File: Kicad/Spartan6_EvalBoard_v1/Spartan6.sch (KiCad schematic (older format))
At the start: 0 parts

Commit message: Schematic almost done
Schematic almost done, just to connect connector to FPGA
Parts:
- added C? (x3): 100n, ~, symbol C
- added C? (x5): 4.7u, ~, symbol C
- added C? (x4): 470n, ~, symbol C
- added C? (x2): 10u, ~, symbol C
- added FB? (x3): F, ~, symbol F
- added P?: CONN_3X2, symbol CONN_3X2
- added Q? (x5): XC6SLX16, Module, symbol XC6SLX16
- added R? (x2): 1K, ~, symbol R
- added R?: 10K, ~, symbol R
- added U?: FM25V05, ~, symbol FM25V05
- added U?: MX25L8006E, ~, symbol MX25L8006E
- added X?: XOSC, symbol XOSC
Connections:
- net labels added: +1.2V, +3.3V, CLK, FLASH_CSn, FLASH_MISO, FLASH_MOSI, FLASH_SCK, GND, I2C_EE_SCL, I2C_EE_SDA, LED1, LED2, LED3, LED4, TCK, TDI, TDO, TMS
- wire segments 0 -> 154

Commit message: Schematic and netllist created
The correct fpga connection to connector will have to be carried out.
Some more footprints need to be created.
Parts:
- removed Q? (x5): XC6SLX16, Module, symbol XC6SLX16
- added Q401: XC6SLX16, Module, symbol XC6SLX16
- gave numbers to parts that had none: 24
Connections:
- net labels added: 1.2V, 3.3V, IO1, IO10, IO11, IO12, IO13, IO14, IO15, IO16, IO17, IO18, IO19, IO2, IO20, IO21, IO22, IO23, IO24, IO25, IO26, IO27, IO28, IO29, IO3, IO30, IO31, IO32, IO33, IO34, IO35, IO36, IO37, IO38, IO39, IO4, IO40, IO41, IO42, IO43, IO44, IO45, IO46, IO47, IO48, IO49, IO5, IO50, IO51, IO52, IO53, IO54, IO55, IO56, IO57, IO58, IO59, IO6, IO60, IO61, IO62, IO63, IO64, IO65, IO66, IO67, IO68, IO69, IO7, IO70, IO8, IO9, IO[1..70]
- net labels removed: +1.2V, +3.3V
- wire segments 154 -> 223
- no-connect marks 0 -> 81
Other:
- moved on the sheet: C401, C402, C403, C404, C405, C406, C407, C408, C409, C410, C411, C412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

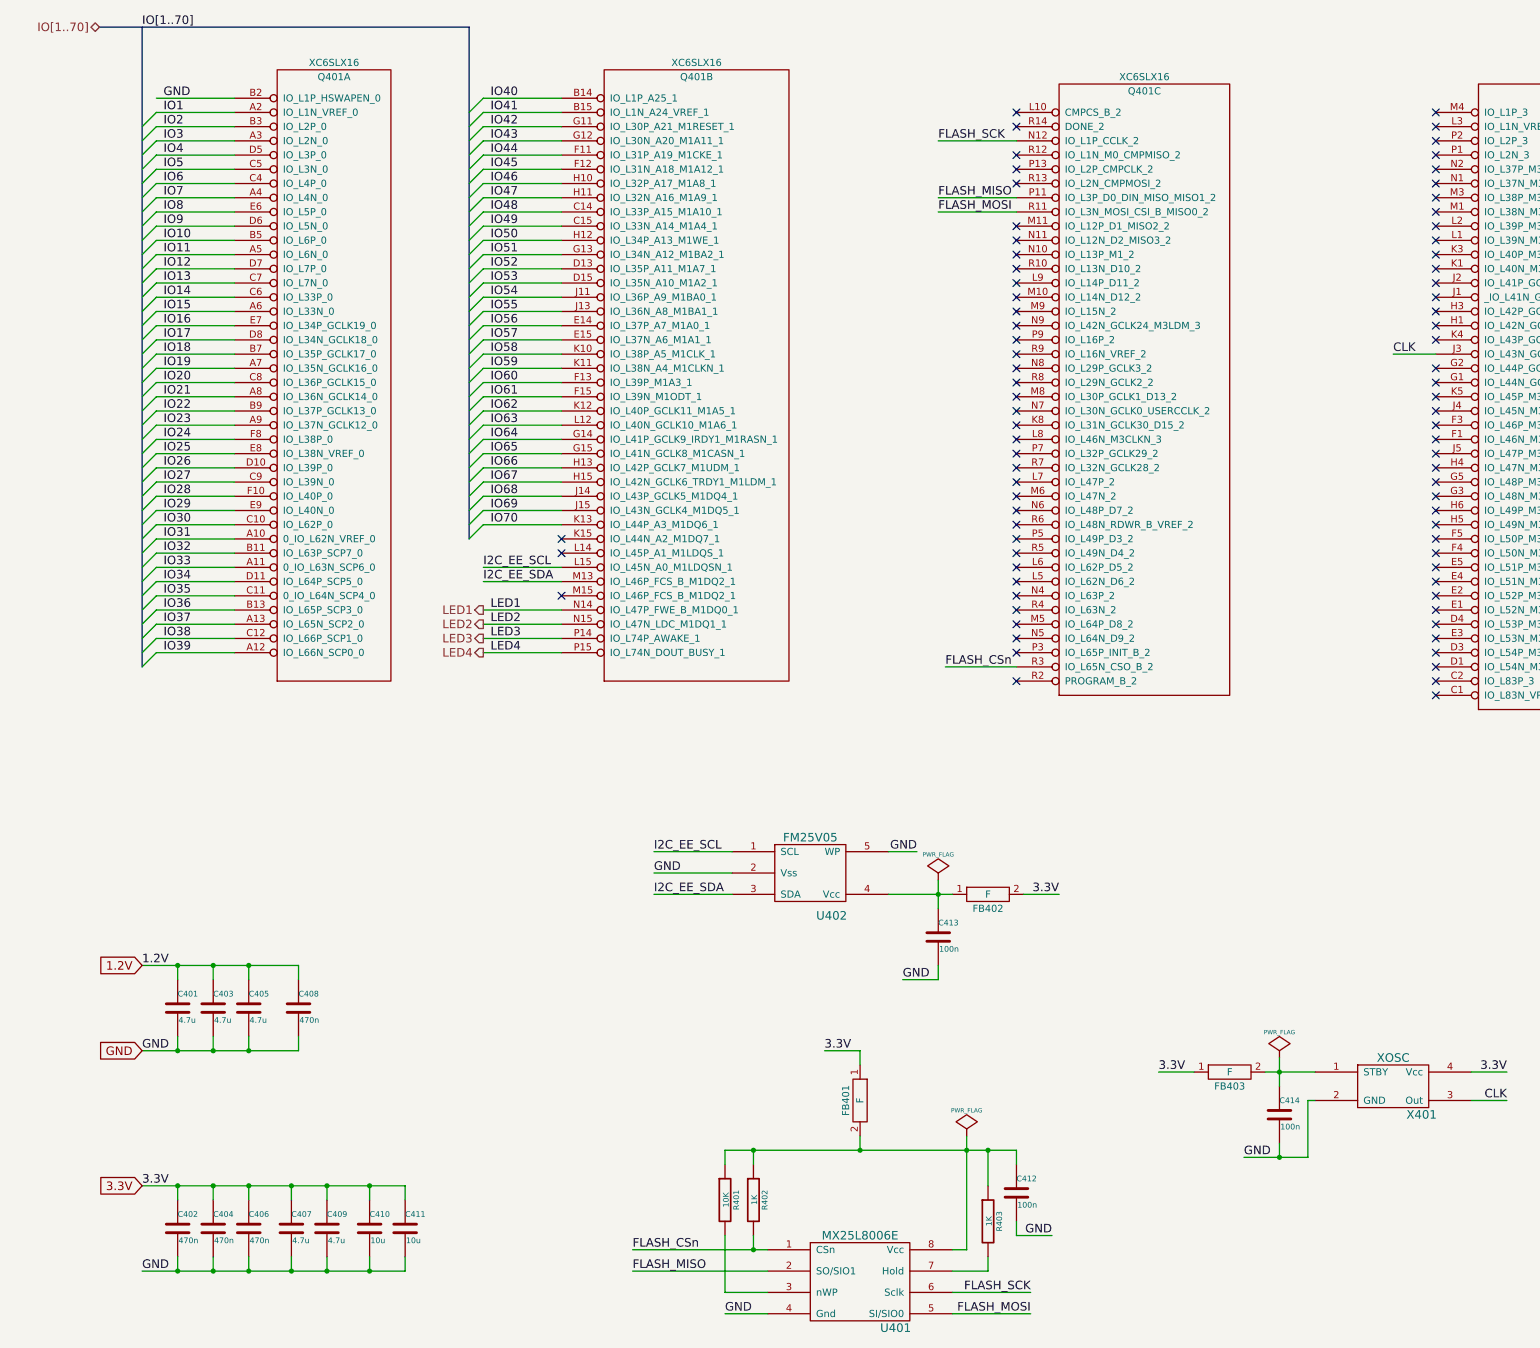
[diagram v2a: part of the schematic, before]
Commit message: Schematic completed, layout starte
Schematic completed, layout starte
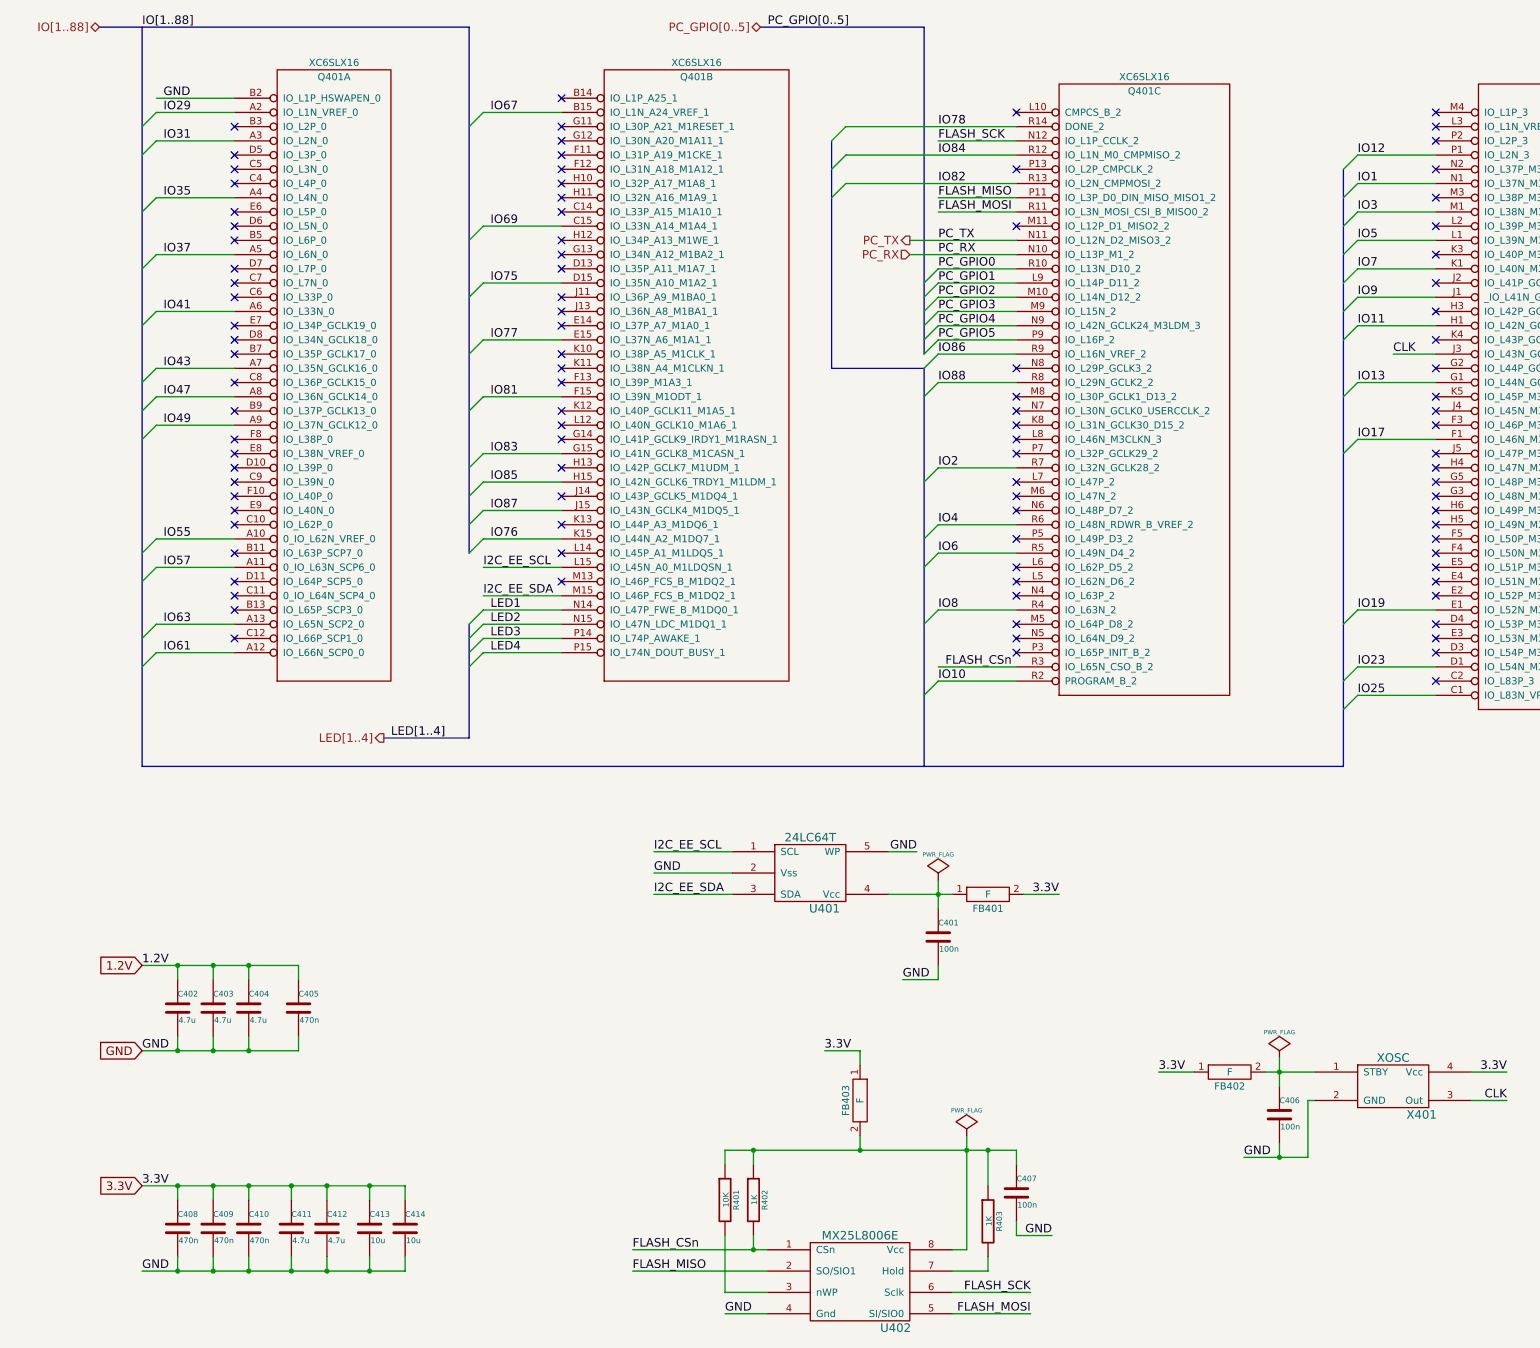
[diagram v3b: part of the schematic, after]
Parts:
- removed U402: FM25V05, ~, symbol FM25V05
- added U401: 24LC64T, symbol 24LC64T
- renumbered C413 to C401, C401 to C402, C405 to C404, C408 to C405, C414 to C406, C412 to C407, C402 to C408, C404 to C409, C406 to C410, C407 to C411, C409 to C412, C410 to C413, C411 to C414, FB402 to FB401, FB403 to FB402, FB401 to FB403, U401 to U402
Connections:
- net IO15 is gone; now on net IO41: Q401.A6 (IO_L33N_0)
- net IO21 is gone; now on net IO47: Q401.A8 (IO_L36N_GCLK14_0)
- net IO33 is gone; now on net IO57: Q401.A11 (0_IO_L63N_SCP6_0)
- net IO39 is gone; now on net IO61: Q401.A12 (IO_L66N_SCP0_0)
- net 1.2V: now also Q401.F9 (VCCINT), Q401.G6 (VCCINT), Q401.G8 (VCCINT), Q401.H9 (VCCINT), Q401.J10 (VCCINT), Q401.J8 (VCCINT), Q401.K7 (VCCINT), Q401.h7 (VCCINT); no longer Q401.F9 (VCCINT), Q401.G6 (VCCINT), Q401.G8 (VCCINT), Q401.H9 (VCCINT), Q401.J10 (VCCINT), Q401.J8 (VCCINT), Q401.K7 (VCCINT), Q401.h7 (VCCINT)
- net 3.3V: now also Q401.B1 (VCCAUX), Q401.B12 (VCCO_0), Q401.B4 (VCCO_0), Q401.B8 (VCCO_0), Q401.D14 (VCCO_1), Q401.D2 (VCCO_3), Q401.D9 (VCCO_0), Q401.E12 (VCCAUX), Q401.F7 (VCCAUX), Q401.G10 (VCCAUX), Q401.G4 (VCCO_3), Q401.H14 (VCCO_1), Q401.H2 (VCCO_3), Q401.J12 (VCCO_1), Q401.J6 (VCCAUX), Q401.K9 (VCCAUX), Q401.L4 (VCCAUX), Q401.M12 (VCCAUX), Q401.M14 (VCCO_1), Q401.M2 (VCCO_3), Q401.M7 (VCCO_2), Q401.P12 (VCCO_2), Q401.P4 (VCCO_2), Q401.P8 (VCCO_2); no longer Q401.B1 (VCCAUX), Q401.B12 (VCCO_0), Q401.B4 (VCCO_0), Q401.B8 (VCCO_0), Q401.D14 (VCCO_1), Q401.D2 (VCCO_3), Q401.D9 (VCCO_0), Q401.E12 (VCCAUX), Q401.F7 (VCCAUX), Q401.G10 (VCCAUX), Q401.G4 (VCCO_3), Q401.H14 (VCCO_1), Q401.H2 (VCCO_3), Q401.J12 (VCCO_1), Q401.J6 (VCCAUX), Q401.K9 (VCCAUX), Q401.L4 (VCCAUX), Q401.M12 (VCCAUX), Q401.M14 (VCCO_1), Q401.M2 (VCCO_3), Q401.M7 (VCCO_2), Q401.P12 (VCCO_2), Q401.P4 (VCCO_2), Q401.P8 (VCCO_2)
- net CLK: now also Q401.J3 (IO_L43N_GCLK22_IRDY2_M3CASN_3); no longer Q401.J3 (IO_L43N_GCLK22_IRDY2_M3CASN_3)
- net FLASH_CSn: now also Q401.R3 (IO_L65N_CSO_B_2); no longer Q401.R3 (IO_L65N_CSO_B_2)
- net FLASH_MISO: now also Q401.P11 (IO_L3P_D0_DIN_MISO_MISO1_2); no longer Q401.P11 (IO_L3P_D0_DIN_MISO_MISO1_2)
- net FLASH_MOSI: now also Q401.R11 (IO_L3N_MOSI_CSI_B_MISO0_2); no longer Q401.R11 (IO_L3N_MOSI_CSI_B_MISO0_2)
- net FLASH_SCK: now also Q401.N12 (IO_L1P_CCLK_2); no longer Q401.N12 (IO_L1P_CCLK_2)
- net GND: now also Q401.A1 (GND), Q401.A15 (GND), Q401.B10 (GND), Q401.B6 (GND), Q401.C13 (GND), Q401.C3 (GND), Q401.E11 (GND), Q401.F14 (GND), Q401.F2 (GND), Q401.F6 (GND), Q401.G7 (GND), Q401.G9 (GND), Q401.H8 (GND), Q401.J7 (GND), Q401.J9 (GND), Q401.K14 (GND), Q401.K2 (GND), Q401.K6 (GND), Q401.L11 (GND), Q401.L13 (SUSPEND), Q401.N13 (GND), Q401.N3 (GND), Q401.P10 (GND), Q401.P6 (GND), Q401.R1 (GND), Q401.R15 (GND), U401.2 (Vss), U401.5 (WP); no longer Q401.A1 (GND), Q401.A15 (GND), Q401.B10 (GND), Q401.B6 (GND), Q401.C13 (GND), Q401.C3 (GND), Q401.E11 (GND), Q401.F14 (GND), Q401.F2 (GND), Q401.F6 (GND), Q401.G7 (GND), Q401.G9 (GND), Q401.H8 (GND), Q401.J7 (GND), Q401.J9 (GND), Q401.K14 (GND), Q401.K2 (GND), Q401.K6 (GND), Q401.L11 (GND), Q401.L13 (SUSPEND), Q401.N13 (GND), Q401.N3 (GND), Q401.P10 (GND), Q401.P6 (GND), Q401.R1 (GND), Q401.R15 (GND)
- net I2C_EE_SCL: now also U401.1 (SCL)
- net I2C_EE_SDA: now also Q401.M15 (IO_L46P_FCS_B_M1DQ2_1), U401.3 (SDA); no longer Q401.M13 (IO_L46P_FCS_B_M1DQ2_1)
- net IO1: now also Q401.N1 (IO_L37N_M3DQ1_3); no longer Q401.A2 (IO_L1N_VREF_0)
- net IO10: now also Q401.R2 (PROGRAM_B_2); no longer Q401.B5 (IO_L6P_0)
- net IO11: now also Q401.H1 (IO_L42N_GCLK24_M3LDM_3); no longer Q401.A5 (IO_L6N_0)
- net IO12: now also Q401.P1 (IO_L2N_3); no longer Q401.D7 (IO_L7P_0)
- net IO13: now also Q401.G1 (IO_L44N_GCLK20_M3A6_3); no longer Q401.C7 (IO_L7N_0)
- net IO17: now also Q401.F1 (IO_L46N_M3CLKN_3); no longer Q401.D8 (IO_L34N_GCLK18_0)
- net IO19: now also Q401.E1 (IO_L52N_M3A9_3); no longer Q401.A7 (IO_L35N_GCLK16_0)
- net IO2: now also Q401.R7 (IO_L32N_GCLK28_2); no longer Q401.B3 (IO_L2P_0)
- net IO23: now also Q401.D1 (IO_L54N_M3A11_3); no longer Q401.A9 (IO_L37N_GCLK12_0)
- net IO25: now also Q401.C1 (IO_L83N_VREF_3); no longer Q401.E8 (IO_L38N_VREF_0)
- net IO29: now also Q401.A2 (IO_L1N_VREF_0); no longer Q401.E9 (IO_L40N_0)
- net IO3: now also Q401.M1 (IO_L38N_M3DQ3_3); no longer Q401.A3 (IO_L2N_0)
- net IO31: now also Q401.A3 (IO_L2N_0); no longer Q401.A10 (0_IO_L62N_VREF_0)
- net IO35: now also Q401.A4 (IO_L4N_0); no longer Q401.C11 (0_IO_L64N_SCP4_0)
- net IO37: now also Q401.A5 (IO_L6N_0); no longer Q401.A13 (IO_L65N_SCP2_0)
- net IO4: now also Q401.R6 (IO_L48N_RDWR_B_VREF_2); no longer Q401.D5 (IO_L3P_0)
- net IO41: no longer Q401.B15 (IO_L1N_A24_VREF_1)
- net IO43: now also Q401.A7 (IO_L35N_GCLK16_0); no longer Q401.G12 (IO_L30N_A20_M1A11_1)
- net IO47: no longer Q401.H11 (IO_L32N_A16_M1A9_1)
- net IO49: now also Q401.A9 (IO_L37N_GCLK12_0); no longer Q401.C15 (IO_L33N_A14_M1A4_1)
- net IO5: now also Q401.L1 (IO_L39N_M3LDQSN_3); no longer Q401.C5 (IO_L3N_0)
- net IO55: now also Q401.A10 (0_IO_L62N_VREF_0); no longer Q401.J13 (IO_L36N_A8_M1BA1_1)
- net IO57: no longer Q401.E15 (IO_L37N_A6_M1A1_1)
- net IO6: now also Q401.R5 (IO_L49N_D4_2); no longer Q401.C4 (IO_L4P_0)
- net IO61: no longer Q401.F15 (IO_L39N_M1ODT_1)
- net IO63: now also Q401.A13 (IO_L65N_SCP2_0); no longer Q401.L12 (IO_L40N_GCLK10_M1A6_1)
- net IO67: now also Q401.B15 (IO_L1N_A24_VREF_1); no longer Q401.H15 (IO_L42N_GCLK6_TRDY1_M1LDM_1)
- net IO69: now also Q401.C15 (IO_L33N_A14_M1A4_1); no longer Q401.J15 (IO_L43N_GCLK4_M1DQ5_1)
- net IO7: now also Q401.K1 (IO_L40N_M3DQ7_3); no longer Q401.A4 (IO_L4N_0)
- net IO8: now also Q401.R4 (IO_L63N_2); no longer Q401.E6 (IO_L5P_0)
- net IO9: now also Q401.J1 (_IO_L41N_GCLK26_M3DQ5_3); no longer Q401.D6 (IO_L5N_0)
- net TCK: now also Q401.A14 (TCK); no longer Q401.A14 (TCK)
- net TDI: now also Q401.E10 (TDI); no longer Q401.E10 (TDI)
- net TDO: now also Q401.D12 (TDO); no longer Q401.D12 (TDO)
- net TMS: now also Q401.E13 (TMS); no longer Q401.E13 (TMS)
- net at C401.1, FB401.1: now also U401.4 (Vcc)
- net IO76: now reaches Q401.K15 (IO_L44N_A2_M1DQ7_1)
- net IO14: no longer names the net of Q401.C6 (IO_L33P_0)
- net IO16: no longer names the net of Q401.E7 (IO_L34P_GCLK19_0)
- net IO18: no longer names the net of Q401.B7 (IO_L35P_GCLK17_0)
- net IO20: no longer names the net of Q401.C8 (IO_L36P_GCLK15_0)
- net IO22: no longer names the net of Q401.B9 (IO_L37P_GCLK13_0)
- net IO24: no longer names the net of Q401.F8 (IO_L38P_0)
- net IO26: no longer names the net of Q401.D10 (IO_L39P_0)
- net IO27: no longer names the net of Q401.C9 (IO_L39N_0)
- net IO28: no longer names the net of Q401.F10 (IO_L40P_0)
- net IO30: no longer names the net of Q401.C10 (IO_L62P_0)
- net IO32: no longer names the net of Q401.B11 (IO_L63P_SCP7_0)
- net IO34: no longer names the net of Q401.D11 (IO_L64P_SCP5_0)
- net IO36: no longer names the net of Q401.B13 (IO_L65P_SCP3_0)
- net IO38: no longer names the net of Q401.C12 (IO_L66P_SCP1_0)
- net IO40: no longer names the net of Q401.B14 (IO_L1P_A25_1)
- net IO42: no longer names the net of Q401.G11 (IO_L30P_A21_M1RESET_1)
- net IO44: no longer names the net of Q401.F11 (IO_L31P_A19_M1CKE_1)
- net IO45: no longer names the net of Q401.F12 (IO_L31N_A18_M1A12_1)
- net IO46: no longer names the net of Q401.H10 (IO_L32P_A17_M1A8_1)
- net IO48: no longer names the net of Q401.C14 (IO_L33P_A15_M1A10_1)
- net IO50: no longer names the net of Q401.H12 (IO_L34P_A13_M1WE_1)
- net IO51: no longer names the net of Q401.G13 (IO_L34N_A12_M1BA2_1)
- net IO52: no longer names the net of Q401.D13 (IO_L35P_A11_M1A7_1)
- net IO53 renamed IO75
- net IO54: no longer names the net of Q401.J11 (IO_L36P_A9_M1BA0_1)
- net IO56: no longer names the net of Q401.E14 (IO_L37P_A7_M1A0_1)
- net IO58: no longer names the net of Q401.K10 (IO_L38P_A5_M1CLK_1)
- net IO59: no longer names the net of Q401.K11 (IO_L38N_A4_M1CLKN_1)
- net IO60: no longer names the net of Q401.F13 (IO_L39P_M1A3_1)
- net IO62: no longer names the net of Q401.K12 (IO_L40P_GCLK11_M1A5_1)
- net IO64: no longer names the net of Q401.G14 (IO_L41P_GCLK9_IRDY1_M1RASN_1)
- net IO65 renamed IO83
- net IO66: no longer names the net of Q401.H13 (IO_L42P_GCLK7_M1UDM_1)
- net IO68: no longer names the net of Q401.J14 (IO_L43P_GCLK5_M1DQ4_1)
- net IO70: no longer names the net of Q401.K13 (IO_L44P_A3_M1DQ6_1)
- new net IO77: Q401.E15 (IO_L37N_A6_M1A1_1)
- new net IO78: Q401.R14 (DONE_2)
- new net IO81: Q401.F15 (IO_L39N_M1ODT_1)
- new net IO82: Q401.R13 (IO_L2N_CMPMOSI_2)
- new net IO84: Q401.R12 (IO_L1N_M0_CMPMISO_2)
- new net IO85: Q401.H15 (IO_L42N_GCLK6_TRDY1_M1LDM_1)
- new net IO86: Q401.R9 (IO_L16N_VREF_2)
- new net IO87: Q401.J15 (IO_L43N_GCLK4_M1DQ5_1)
- new net IO88: Q401.R8 (IO_L29N_GCLK2_2)
- new net PC_GPIO0: Q401.R10 (IO_L13N_D10_2)
- new net PC_GPIO1: Q401.L9 (IO_L14P_D11_2)
- new net PC_GPIO2: Q401.M10 (IO_L14N_D12_2)
- new net PC_GPIO3: Q401.M9 (IO_L15N_2)
- new net PC_GPIO4: Q401.N9 (IO_L42N_GCLK24_M3LDM_3)
- new net PC_GPIO5: Q401.P9 (IO_L16P_2)
- new net PC_RX: Q401.N10 (IO_L13P_M1_2)
- new net PC_TX: Q401.N11 (IO_L12N_D2_MISO3_2)
- no-connect marks 81 -> 100
